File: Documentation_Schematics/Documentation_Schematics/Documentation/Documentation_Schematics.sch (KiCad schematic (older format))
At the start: 19 parts

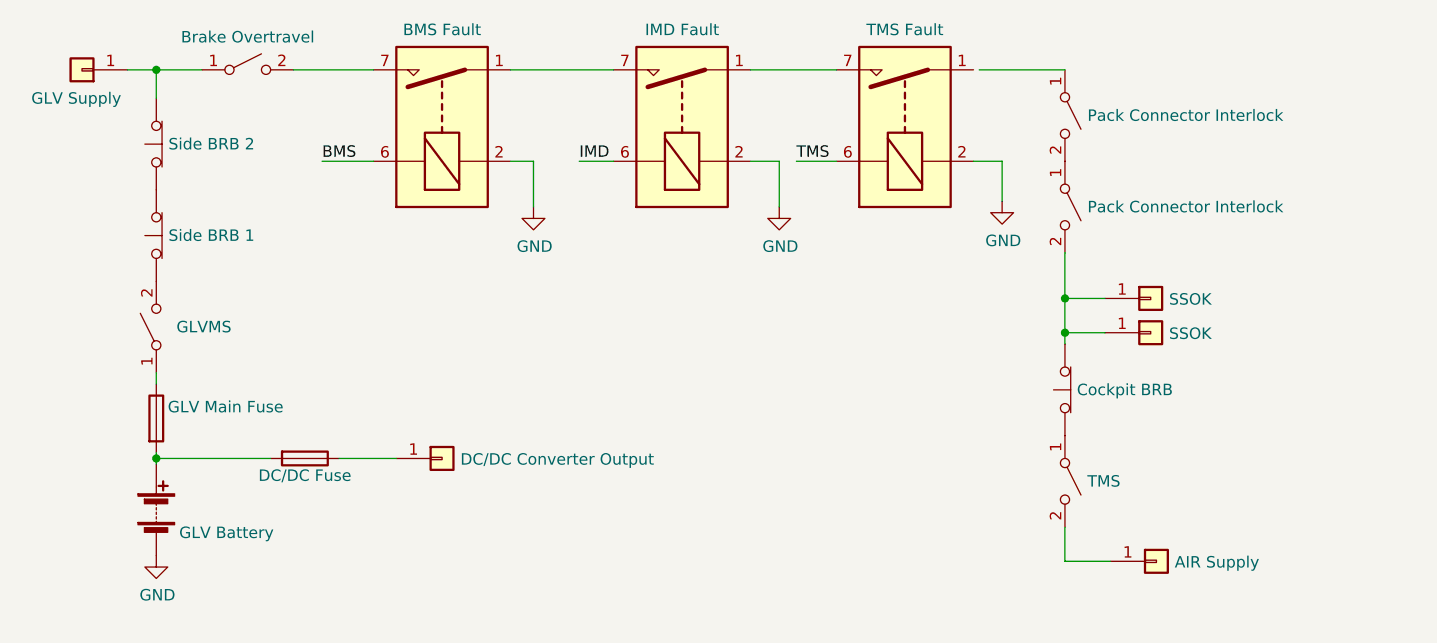
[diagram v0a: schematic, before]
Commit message: added documentaiton
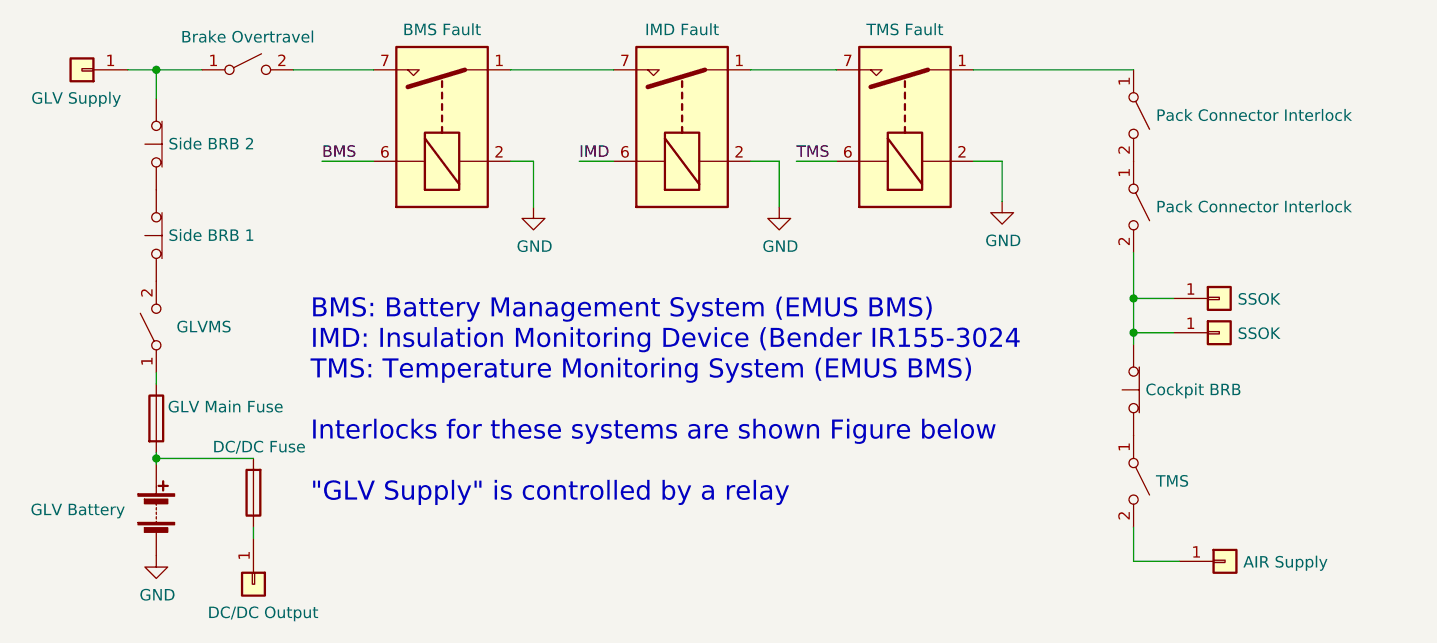
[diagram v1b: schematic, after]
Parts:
- J?: value DC/DC Converter Output -> DC/DC Output
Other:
- note added: "BMS: Battery Management System (EMUS BMS)\nIMD: Insulation Monitoring Device (Bender IR155-3024\nTMS: Temperature Monitoring System (EMUS BMS)\n\nInterlocks for these systems are shown Figure below\n\n"GLV Supply" is controlled by a relay"
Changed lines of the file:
@@
 L Switch:SW_SPST SW?
 U 1 1 5F912643
-P 6275 2450
-F 0 "SW?" V 6229 2548 50  0001 L CNN
-F 1 "Pack Connector Interlock" V 6275 2548 50  0000 L CNN
-F 2 "" H 6275 2450 50  0001 C CNN
-F 3 "~" H 6275 2450 50  0001 C CNN
-	1    6275 2450
+P 6575 2450
+F 0 "SW?" V 6529 2548 50  0001 L CNN
+F 1 "Pack Connector Interlock" V 6575 2548 50  0000 L CNN
+F 2 "" H 6575 2450 50  0001 C CNN
+F 3 "~" H 6575 2450 50  0001 C CNN
+	1    6575 2450
 	0    1    1    0
 $EndComp
@@
 L Switch:SW_SPST SW?
 U 1 1 5F912EE1
-P 6275 2850
-F 0 "SW?" V 6229 2948 50  0001 L CNN
-F 1 "Pack Connector Interlock" V 6275 2948 50  0000 L CNN
-F 2 "" H 6275 2850 50  0001 C CNN
-F 3 "~" H 6275 2850 50  0001 C CNN
-	1    6275 2850
+P 6575 2850
+F 0 "SW?" V 6529 2948 50  0001 L CNN
+F 1 "Pack Connector Interlock" V 6575 2948 50  0000 L CNN
+F 2 "" H 6575 2850 50  0001 C CNN
+F 3 "~" H 6575 2850 50  0001 C CNN
+	1    6575 2850
 	0    1    1    0
 $EndComp
@@
 L Connector_Generic:Conn_01x01 J?
 U 1 1 5F913410
-P 6650 3250
-F 0 "J?" H 6730 3292 50  0001 L CNN
-F 1 "SSOK" H 6730 3246 50  0000 L CNN
-F 2 "" H 6650 3250 50  0001 C CNN
-F 3 "~" H 6650 3250 50  0001 C CNN
-	1    6650 3250
+P 6950 3250
+F 0 "J?" H 7030 3292 50  0001 L CNN
+F 1 "SSOK" H 7030 3246 50  0000 L CNN
+F 2 "" H 6950 3250 50  0001 C CNN
+F 3 "~" H 6950 3250 50  0001 C CNN
+	1    6950 3250
 	1    0    0    -1
 $EndComp
@@
 L Switch:SW_Push_Open SW?
 U 1 1 5F914DC3
-P 6275 3650
-F 0 "SW?" V 6321 3598 50  0001 R CNN
-F 1 "Cockpit BRB" V 6275 3598 50  0000 R CNN
-F 2 "" H 6275 3850 50  0001 C CNN
-F 3 "~" H 6275 3850 50  0001 C CNN
-	1    6275 3650
+P 6575 3650
+F 0 "SW?" V 6621 3598 50  0001 R CNN
+F 1 "Cockpit BRB" V 6575 3598 50  0000 R CNN
+F 2 "" H 6575 3850 50  0001 C CNN
+F 3 "~" H 6575 3850 50  0001 C CNN
+	1    6575 3650
 	0    -1   -1   0
 $EndComp
@@
 L Switch:SW_SPST SW?
 U 1 1 5F91AF7C
-P 6275 4050
-F 0 "SW?" V 6229 4148 50  0001 L CNN
-F 1 "TMS" V 6275 4148 50  0000 L CNN
-F 2 "" H 6275 4050 50  0001 C CNN
-F 3 "~" H 6275 4050 50  0001 C CNN
-	1    6275 4050
+P 6575 4050
+F 0 "SW?" V 6529 4148 50  0001 L CNN
+F 1 "TMS" V 6575 4148 50  0000 L CNN
+F 2 "" H 6575 4050 50  0001 C CNN
+F 3 "~" H 6575 4050 50  0001 C CNN
+	1    6575 4050
 	0    1    1    0
 $EndComp
@@
 L Connector_Generic:Conn_01x01 J?
 U 1 1 5F91B70E
-P 6675 4400
-F 0 "J?" H 6755 4442 50  0001 L CNN
-F 1 "AIR Supply" H 6755 4396 50  0000 L CNN
-F 2 "" H 6675 4400 50  0001 C CNN
-F 3 "~" H 6675 4400 50  0001 C CNN
-	1    6675 4400
+P 6975 4400
+F 0 "J?" H 7055 4442 50  0001 L CNN
+F 1 "AIR Supply" H 7055 4396 50  0000 L CNN
+F 2 "" H 6975 4400 50  0001 C CNN
+F 3 "~" H 6975 4400 50  0001 C CNN
+	1    6975 4400
 	1    0    0    -1
 $EndComp
@@
 	4900 2250 5275 2250
 Wire Wire Line
-	5900 2250 6275 2250
-Wire Wire Line
-	6275 3050 6275 3250
-Wire Wire Line
-	6275 3250 6450 3250
-Wire Wire Line
-	6275 3250 6275 3400
-Connection ~ 6275 3250
-Wire Wire Line
-	6275 4250 6275 4400
-Wire Wire Line
-	6275 4400 6475 4400
+	6575 3050 6575 3250
+Wire Wire Line
+	6575 3250 6750 3250
+Wire Wire Line
+	6575 3250 6575 3400
+Connection ~ 6575 3250
+Wire Wire Line
+	6575 4250 6575 4400
+Wire Wire Line
+	6575 4400 6775 4400
 Wire Wire Line
 	5875 2650 6000 2650
@@
 L Device:Fuse F?
 U 1 1 5F92A12A
-P 2950 3950
-F 0 "F?" V 2753 3950 50  0001 C CNN
-F 1 "DC/DC Fuse" V 3025 3950 50  0000 C CNN
-F 2 "" V 2880 3950 50  0001 C CNN
-F 3 "~" H 2950 3950 50  0001 C CNN
-	1    2950 3950
-	0    1    1    0
+P 2725 4100
+F 0 "F?" V 2528 4100 50  0001 C CNN
+F 1 "DC/DC Fuse" H 2700 3900 50  0000 C CNN
+F 2 "" V 2655 4100 50  0001 C CNN
+F 3 "~" H 2725 4100 50  0001 C CNN
+	1    2725 4100
+	-1   0    0    1
 $EndComp
 $Comp
 L Connector_Generic:Conn_01x01 J?
 U 1 1 5F92A6D1
-P 3550 3950
-F 0 "J?" H 3630 3992 50  0001 L CNN
-F 1 "DC/DC Converter Output" H 3630 3946 50  0000 L CNN
-F 2 "" H 3550 3950 50  0001 C CNN
-F 3 "~" H 3550 3950 50  0001 C CNN
-	1    3550 3950
-	1    0    0    -1
-$EndComp
-Wire Wire Line
-	2800 3950 2300 3950
+P 2725 4500
+F 0 "J?" H 2805 4542 50  0001 L CNN
+F 1 "DC/DC Output" V 2850 4300 50  0000 L CNN
+F 2 "" H 2725 4500 50  0001 C CNN
+F 3 "~" H 2725 4500 50  0001 C CNN
+	1    2725 4500
+	0    1    1    0
+$EndComp
+Wire Wire Line
+	2725 3950 2300 3950
 Connection ~ 2300 3950
 Wire Wire Line
@@
 P 2300 4175
 F 0 "BT?" H 2408 4221 50  0001 L CNN
-F 1 "GLV Battery" H 2400 4075 50  0000 L CNN
+F 1 "GLV Battery" H 1750 4175 50  0000 L CNN
 F 2 "" V 2300 4235 50  0001 C CNN
 F 3 "~" V 2300 4235 50  0001 C CNN
@@
 	-1   0    0    1
 $EndComp
-Wire Wire Line
-	3350 3950 3100 3950
 $Comp
 L Relay:DIPxx-1Axx-11x K?
@@
 L Connector_Generic:Conn_01x01 J?
 U 1 1 5F93D847
-P 6650 3400
-F 0 "J?" H 6730 3442 50  0001 L CNN
-F 1 "SSOK" H 6730 3396 50  0000 L CNN
-F 2 "" H 6650 3400 50  0001 C CNN
-F 3 "~" H 6650 3400 50  0001 C CNN
-	1    6650 3400
-	1    0    0    -1
-$EndComp
-Wire Wire Line
-	6275 3400 6450 3400
-Connection ~ 6275 3400
-Wire Wire Line
-	6275 3400 6275 3450
+P 6950 3400
+F 0 "J?" H 7030 3442 50  0001 L CNN
+F 1 "SSOK" H 7030 3396 50  0000 L CNN
+F 2 "" H 6950 3400 50  0001 C CNN
+F 3 "~" H 6950 3400 50  0001 C CNN
+	1    6950 3400
+	1    0    0    -1
+$EndComp
+Wire Wire Line
+	6575 3400 6750 3400
+Connection ~ 6575 3400
+Wire Wire Line
+	6575 3400 6575 3450
 Text Label 3025 2650 0    50   ~ 0
 BMS
@@
 Wire Wire Line
 	5100 2650 5275 2650
+Text Notes 2975 4150 0    83   ~ 0
+BMS: Battery Management System (EMUS BMS)\nIMD: Insulation Monitoring Device (Bender IR155-3024\nTMS: Temperature Monitoring System (EMUS BMS)\n\nInterlocks for these systems are shown Figure below\n\n"GLV Supply" is controlled by a relay
+Wire Wire Line
+	2725 4250 2725 4300
+Wire Wire Line
+	5875 2250 6575 2250
 $EndSCHEMATC
